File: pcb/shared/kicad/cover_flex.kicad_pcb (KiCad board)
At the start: 2 copper layers, 31.1 x 30.1 mm, 8 parts, among them J1 +5V pin pad, J2 GND pin pad, J3 S7081-42R VBAT, J4 S7081-42R GND, U1 TLV75533PDBVR

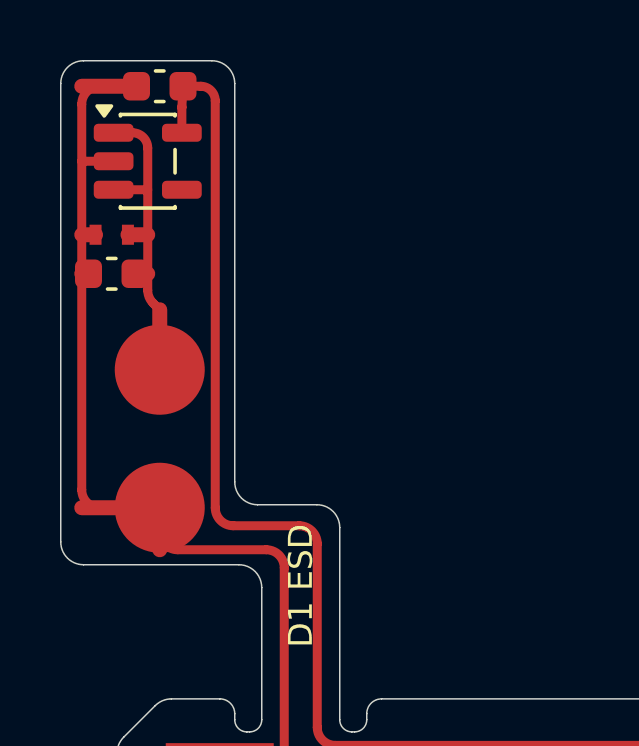
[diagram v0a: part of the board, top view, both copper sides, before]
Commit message: v0.6: one barrier per variant, EU ridges, NA cable slit, ElegooSlicer projects, back cover and plate fixes (D-127..D-150)
- One barrier per variant for every edition; printed blank board in switch only (D-127..D-131)
- EU pin board ridge loop and blank board ridge; more pin board bosses (D-128..D-133)
- NA face plate lobes round the screws form the pocket's ends (D-132)
- NA 5 V cable straight from J2 to J1 through a slit in the barrier's bottom wall, 50 mm FFC; MH3 back in line;
  slit open in battery-free and switch only (D-134, D-135)
- Back cover: flex pad section 1.5 mm in, rim cut at the bottom end with a 0.08 mm-layer taper, steel plate clips
  solid in the shell, bottom clip lead-in 45 deg, pry notch 1.5 deep (D-136..D-143, D-145, D-147)
- 45 deg chamfer round the remote pocket's mouth (D-139)
- Print projects built with ElegooSlicer 1.5.3.5, overrides also as object settings (D-144)
- EU plain face plate 84.6 x 84.6, plain carrier whole on all sides with the full rim (D-146, D-150)
- Steel piece 1.0 mm thick, recess 1.2 deep (D-148)
- MSR-2 12 mm left, grille on the plate's centre line; ant logos in the sensor boards' lower-left corners (D-149)
- Repo URL github.com/antevens/sladdseg on the boards
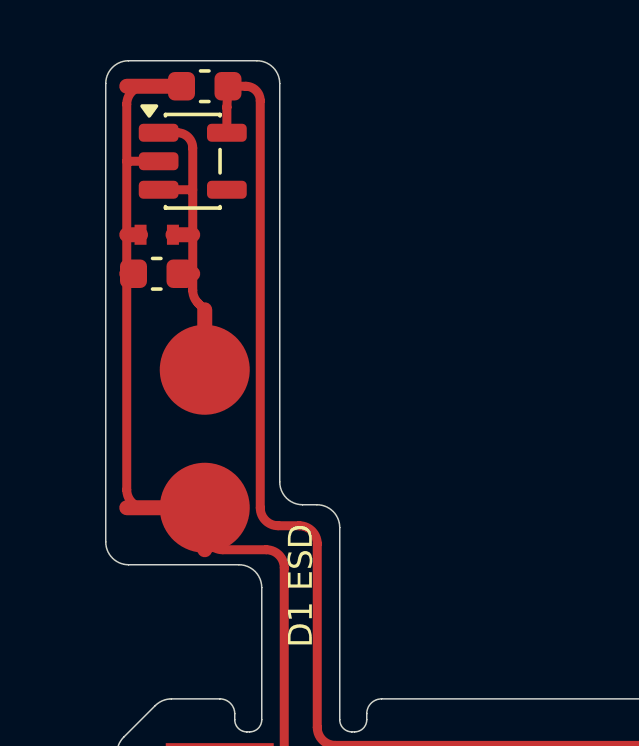
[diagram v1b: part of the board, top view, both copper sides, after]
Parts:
- moved C3 1.50 mm to (86.7, 105.7)
- moved C4 1.50 mm to (88.3, 99.5)
- moved D1 1.50 mm to (86.7, 104.4)
- moved J1 1.50 mm to (88.3, 108.9)
- moved J2 1.50 mm to (88.3, 113.5)
- moved U1 1.50 mm to (87.9, 102.0)
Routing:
- net GND: track 44.8 -> 43.3 mm
- net +3V3: track 52.2 -> 50.7 mm
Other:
- board size 31.1 x 30.1 mm -> 29.6 x 30.1 mm
